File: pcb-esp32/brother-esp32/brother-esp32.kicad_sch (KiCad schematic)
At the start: 77 parts, among them J1 Conn_01x40_Female, U1 SST39SF040-55-4I-WHE, U2 ESP32-DEVKITC_WROOM, U3 MCP23016-I/SO

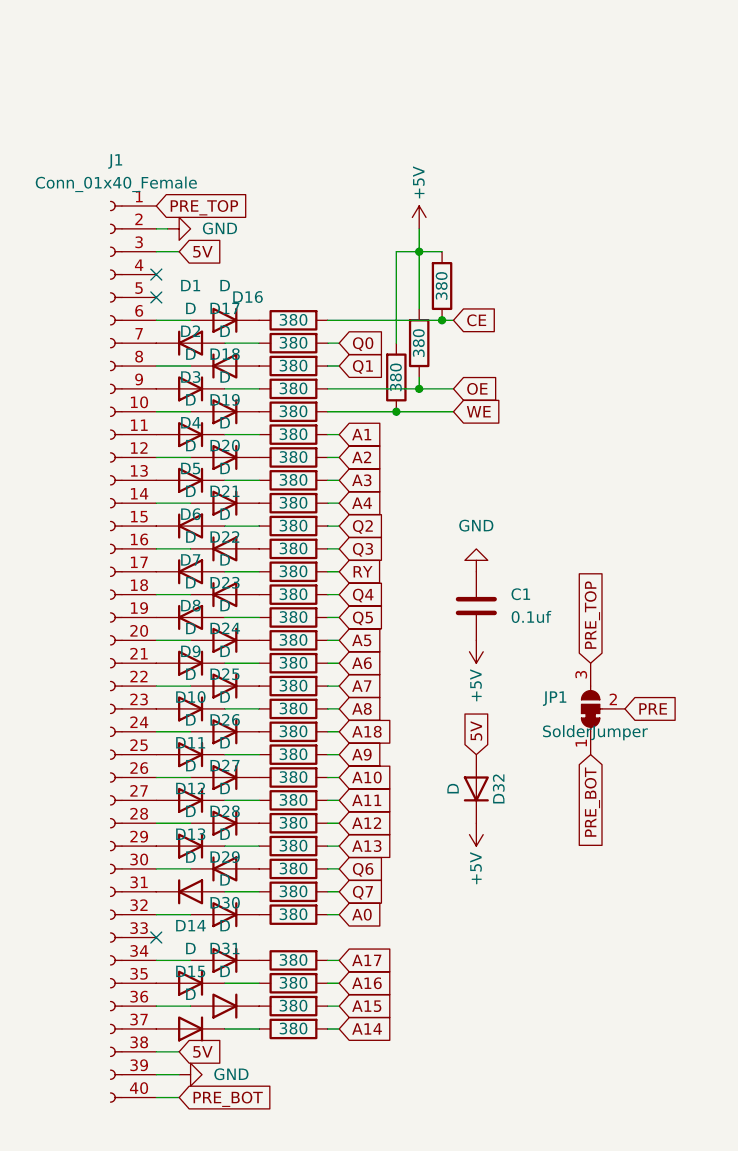
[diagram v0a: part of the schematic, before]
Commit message: Updated design remove diodes
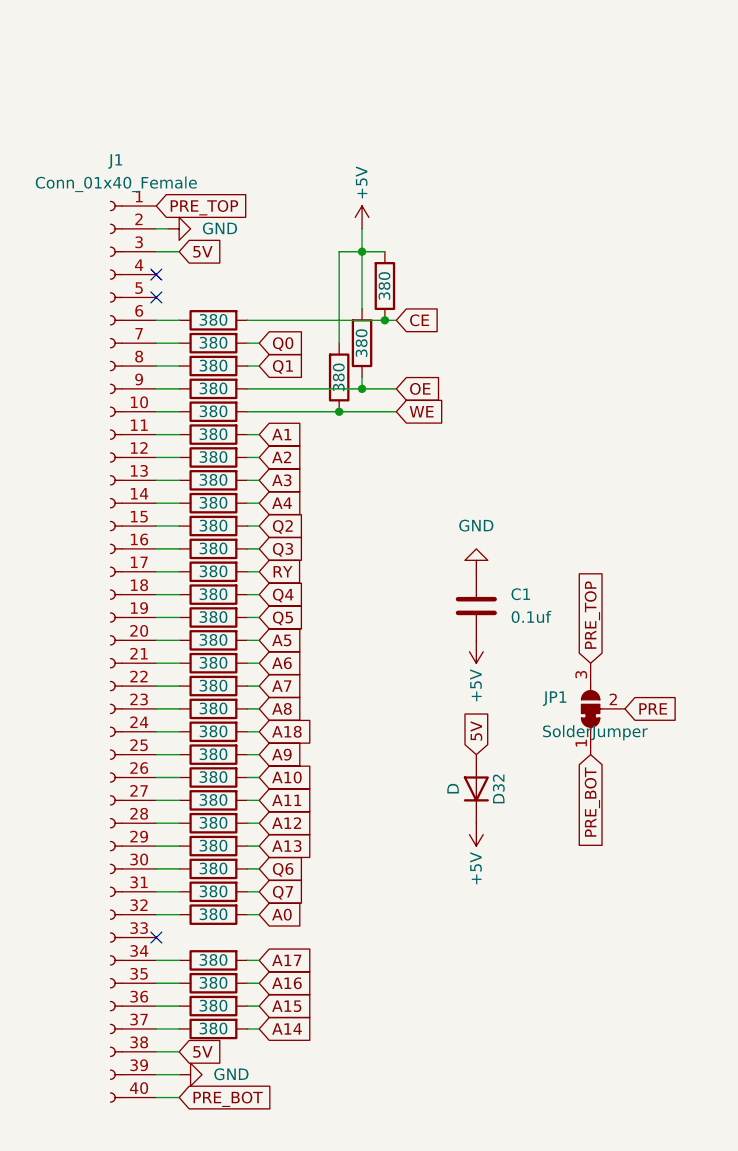
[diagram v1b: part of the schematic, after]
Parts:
- removed D1, D10, D11, D12, D13, D14, D15, D16, D17, D18, D19, D2, D20, D21, D22, D23, D24, D25, D26, D27, D28, D29, D3, D30, D31, D4, D5, D6, D7, D8, D9: D, Diode_SMD:D_SOD-323_HandSoldering, symbol Device:D
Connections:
- net at J1.30 (Pin_30): now also R25.1
- net at R28.1: now also J1.34 (Pin_34)
- net at R20.1: now also J1.25 (Pin_25)
- net at J1.16 (Pin_16): now also R11.1
- net at R23.1: now also J1.28 (Pin_28)
- net at R13.1: now also J1.18 (Pin_18)
- net at R16.1: now also J1.21 (Pin_21)
- net at R17.1: now also J1.22 (Pin_22)
- net at R15.1: now also J1.20 (Pin_20)
- net at R7.1: now also J1.12 (Pin_12)
- net at R12.1: now also J1.17 (Pin_17)
- net at J1.31 (Pin_31): now also R26.1
- net at R22.1: now also J1.27 (Pin_27)
- net at R18.1: now also J1.23 (Pin_23)
- net at R19.1: now also J1.24 (Pin_24)
- net at R29.1: now also J1.35 (Pin_35)
- net at R9.1: now also J1.14 (Pin_14)
- net at R30.1: now also J1.36 (Pin_36)
- net at R8.1: now also J1.13 (Pin_13)
- net at R14.1: now also J1.19 (Pin_19)
- net at J1.7 (Pin_7): now also R2.1
- net at J1.15 (Pin_15): now also R10.1
- net at R27.1: now also J1.32 (Pin_32)
- net at J1.8 (Pin_8): now also R3.1
- net at R5.1: now also J1.10 (Pin_10)
- net at R24.1: now also J1.29 (Pin_29)
- net at R4.1: now also J1.9 (Pin_9)
- net at R31.1: now also J1.37 (Pin_37)
- net at R21.1: now also J1.26 (Pin_26)
- net at J1.11 (Pin_11): now also R6.1
- net at J1.6 (Pin_6): now also R1.1
